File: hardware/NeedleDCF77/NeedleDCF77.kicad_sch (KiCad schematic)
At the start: 42 parts, among them J1 USB_C_Receptacle_USB2.0, U2 STM32L051C8Tx

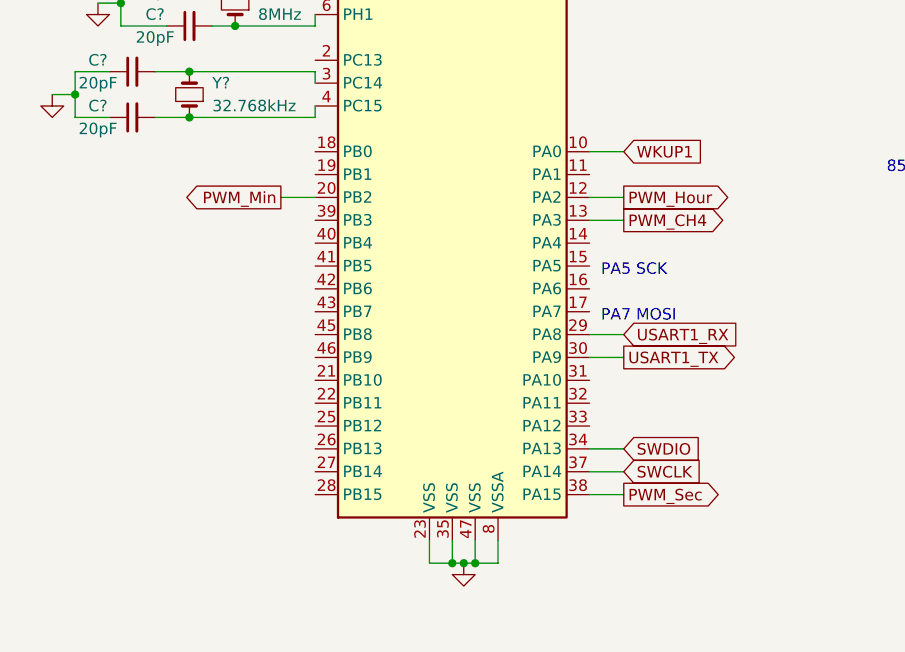
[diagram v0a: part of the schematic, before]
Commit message: Chose correct pins for PWM
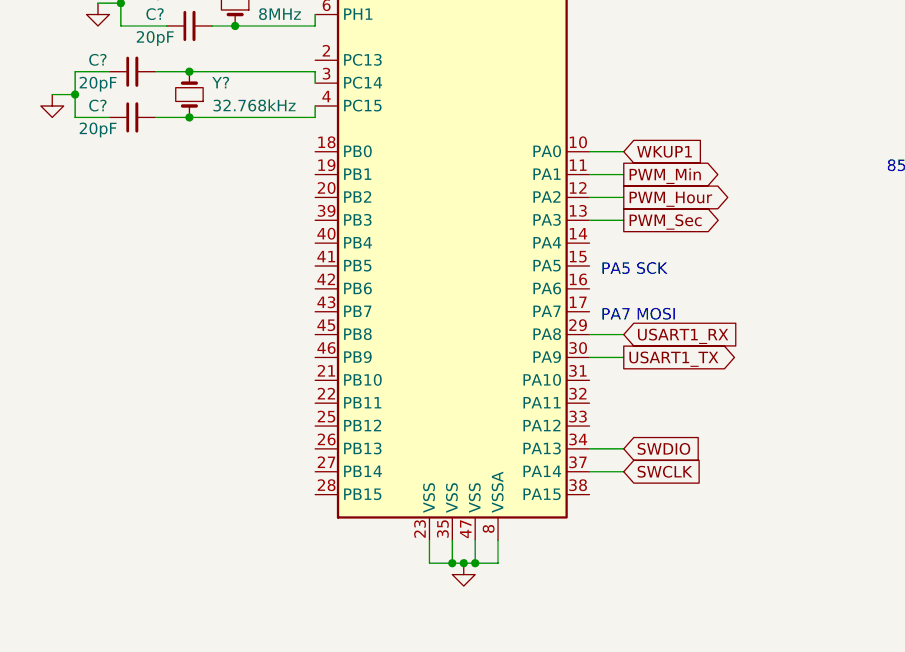
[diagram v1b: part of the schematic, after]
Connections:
- net PWM_CH4 is gone; now on net PWM_Sec: U2.13 (PA3)
- net PWM_Min: now also U2.11 (PA1); no longer U2.20 (PB2)
- net PWM_Sec: no longer U2.38 (PA15)

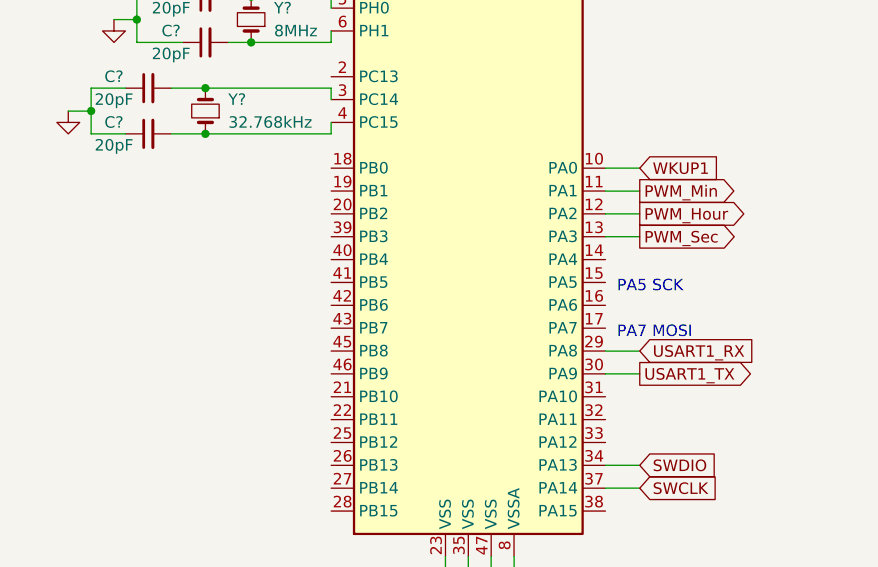
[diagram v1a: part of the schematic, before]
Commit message: Chose correct pins for SPI1
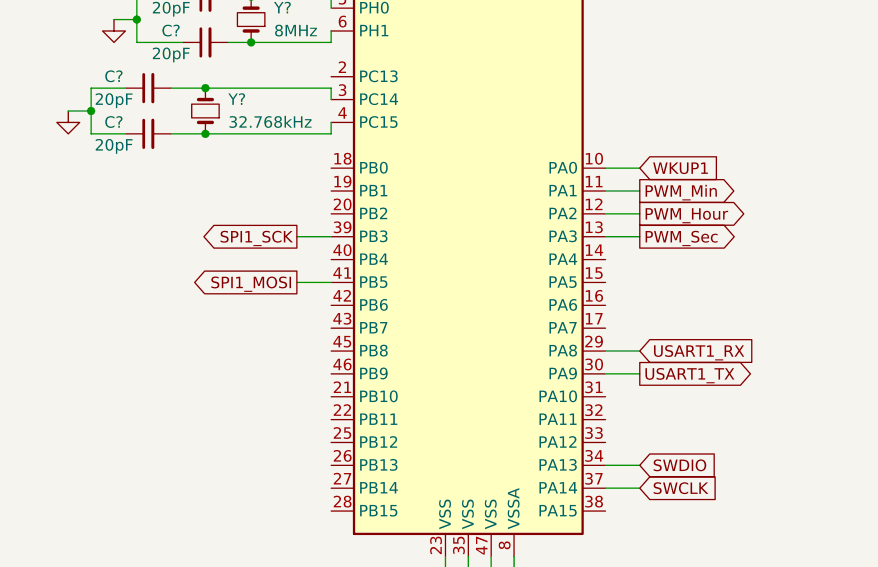
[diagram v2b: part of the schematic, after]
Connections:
- net SPI1_SCK: now reaches U2.39 (PB3)
- net SPI1_MOSI: now reaches U2.41 (PB5)
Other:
- note removed: "PA5 SCK"
- note removed: "PA7 MOSI"
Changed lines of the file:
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@@
+    (stroke (width 0) (type default))
+  )
+  (wire (pts (xy 157.48 147.32) (xy 161.29 147.32))
     (stroke (width 0) (type default))
   )
@@
   )
   (wire (pts (xy 254 152.4) (xy 254 154.94))
+    (stroke (width 0) (type default))
+  )
+  (wire (pts (xy 157.48 142.24) (xy 161.29 142.24))
     (stroke (width 0) (type default))
   )
@@
     (effects (font (size 1.27 1.27)) (justify left bottom))
   )
-  (text "PA5 SCK" (at 193.04 148.59 0)
-    (effects (font (size 1.27 1.27)) (justify left bottom))
-  )
   (text "On second PS create 5V to power VFD filament driver,\n and use linear regulator to 3v3 for ex on DCF77, or pending\n"
     (at 189.23 62.23 0)
     (effects (font (size 1.27 1.27)) (justify left bottom))
   )
-  (text "PA7 MOSI" (at 193.04 153.67 0)
-    (effects (font (size 1.27 1.27)) (justify left bottom))
-  )
   (text "85C1 50uA Resistance ~ 3.33kOma" (at 224.79 137.16 0)
     (effects (font (size 1.27 1.27)) (justify left bottom))
@@
     )
   )
+  (global_label "SPI1_SCK" (shape output) (at 157.48 142.24 180) (fields_autoplaced)
+    (effects (font (size 1.27 1.27)) (justify right))
+    (property "Intersheetrefs" "${INTERSHEET_REFS}" (at 145.5633 142.24 0)
+      (effects (font (size 1.27 1.27)) (justify right) hide)
+    )
+  )
   (global_label "PWM_Hour" (shape input) (at 250.19 139.7 180) (fields_autoplaced)
     (effects (font (size 1.27 1.27)) (justify right))
@@
     )
   )
+  (global_label "SPI1_MOSI" (shape output) (at 157.48 147.32 180) (fields_autoplaced)
+    (effects (font (size 1.27 1.27)) (justify right))
+    (property "Intersheetrefs" "${INTERSHEET_REFS}" (at 144.7166 147.32 0)
+      (effects (font (size 1.27 1.27)) (justify right) hide)
+    )
+  )

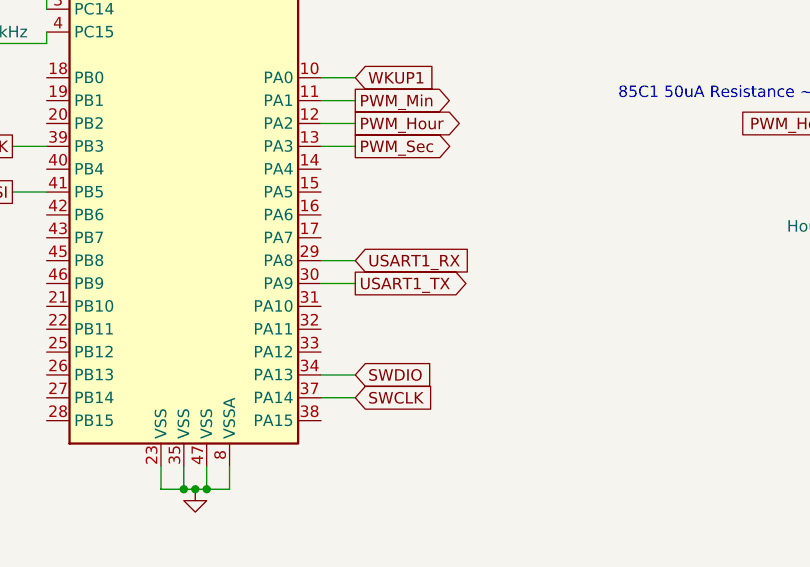
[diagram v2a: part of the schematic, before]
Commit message: Chose correct pins for UART1
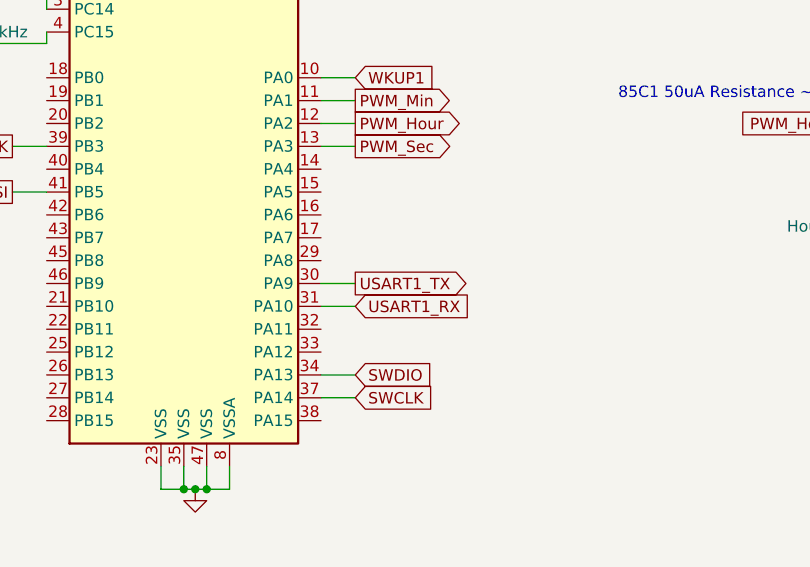
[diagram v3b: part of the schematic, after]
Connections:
- net USART1_RX: now also U2.31 (PA10); no longer U2.29 (PA8)
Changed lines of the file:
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@@
+    (stroke (width 0) (type default))
+  )
+  (wire (pts (xy 191.77 160.02) (xy 195.58 160.02))
     (stroke (width 0) (type default))
   )
@@
   )
   (wire (pts (xy 189.23 36.83) (xy 191.77 36.83))
-    (stroke (width 0) (type default))
-  )
-  (wire (pts (xy 191.77 154.94) (xy 195.58 154.94))
     (stroke (width 0) (type default))
   )
@@
     )
   )
-  (global_label "USART1_RX" (shape input) (at 195.58 154.94 0) (fields_autoplaced)
-    (effects (font (size 1.27 1.27)) (justify left))
-    (property "Intersheetrefs" "${INTERSHEET_REFS}" (at 208.516 154.8606 0)
-      (effects (font (size 1.27 1.27)) (justify left) hide)
-    )
+  (global_label "USART1_RX" (shape input) (at 195.58 160.02 0) (fields_autoplaced)
+    (effects (font (size 1.27 1.27)) (justify left))
+    (property "Intersheetrefs" "${INTERSHEET_REFS}" (at 208.516 159.9406 0)
+      (effects (font (size 1.27 1.27)) (justify left) hide)
+    )

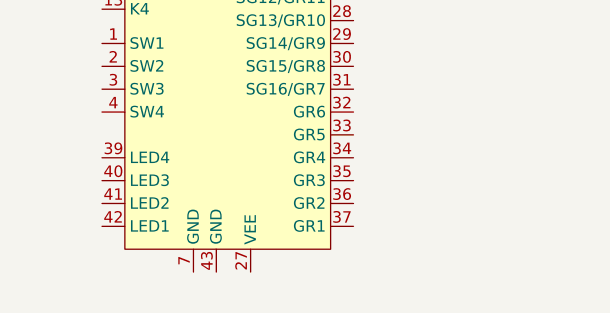
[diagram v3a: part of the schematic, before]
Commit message: Add ground to PT6312
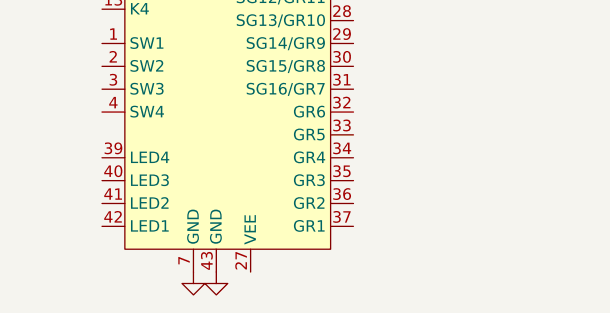
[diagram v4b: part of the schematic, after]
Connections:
- net GND: now also U?.43 (GND), U?.7 (GND)
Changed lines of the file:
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@@
+    )
+  )
+  (symbol (lib_id "power:GND") (at 48.26 187.96 0) (unit 1)
+    (in_bom yes) (on_board yes) (dnp no) (fields_autoplaced)
+    (property "Reference" "#PWR02" (at 48.26 194.31 0)
+      (effects (font (size 1.27 1.27)) hide)
+    )
+    (property "Value" "GND" (at 48.26 193.04 0)
+      (effects (font (size 1.27 1.27)) hide)
+    )
+    (property "Footprint" "" (at 48.26 187.96 0)
+      (effects (font (size 1.27 1.27)) hide)
+    )
+    (property "Datasheet" "" (at 48.26 187.96 0)
+      (effects (font (size 1.27 1.27)) hide)
+    )
+    (pin "1")
+    (instances
+      (project "NeedleDCF77"
+        (path "/9538e4ed-27e6-4c37-b989-9859dc0d49e8"
+          (reference "#PWR02") (unit 1)
+        )
+      )
     )
   )
@@
         )
       )
+    )
+  )
+  (symbol (lib_id "power:GND") (at 45.72 187.96 0) (unit 1)
+    (in_bom yes) (on_board yes) (dnp no) (fields_autoplaced)
+    (property "Reference" "#PWR01" (at 45.72 194.31 0)
+      (effects (font (size 1.27 1.27)) hide)
+    )
+    (property "Value" "GND" (at 45.72 193.04 0)
+      (effects (font (size 1.27 1.27)) hide)
+    )
+    (property "Footprint" "" (at 45.72 187.96 0)
+      (effects (font (size 1.27 1.27)) hide)
+    )
+    (property "Datasheet" "" (at 45.72 187.96 0)
+      (effects (font (size 1.27 1.27)) hide)
+    )
+    (pin "1")
+    (instances
+      (project "NeedleDCF77"
+        (path "/9538e4ed-27e6-4c37-b989-9859dc0d49e8"
+          (reference "#PWR01") (unit 1)
+        )
+      )

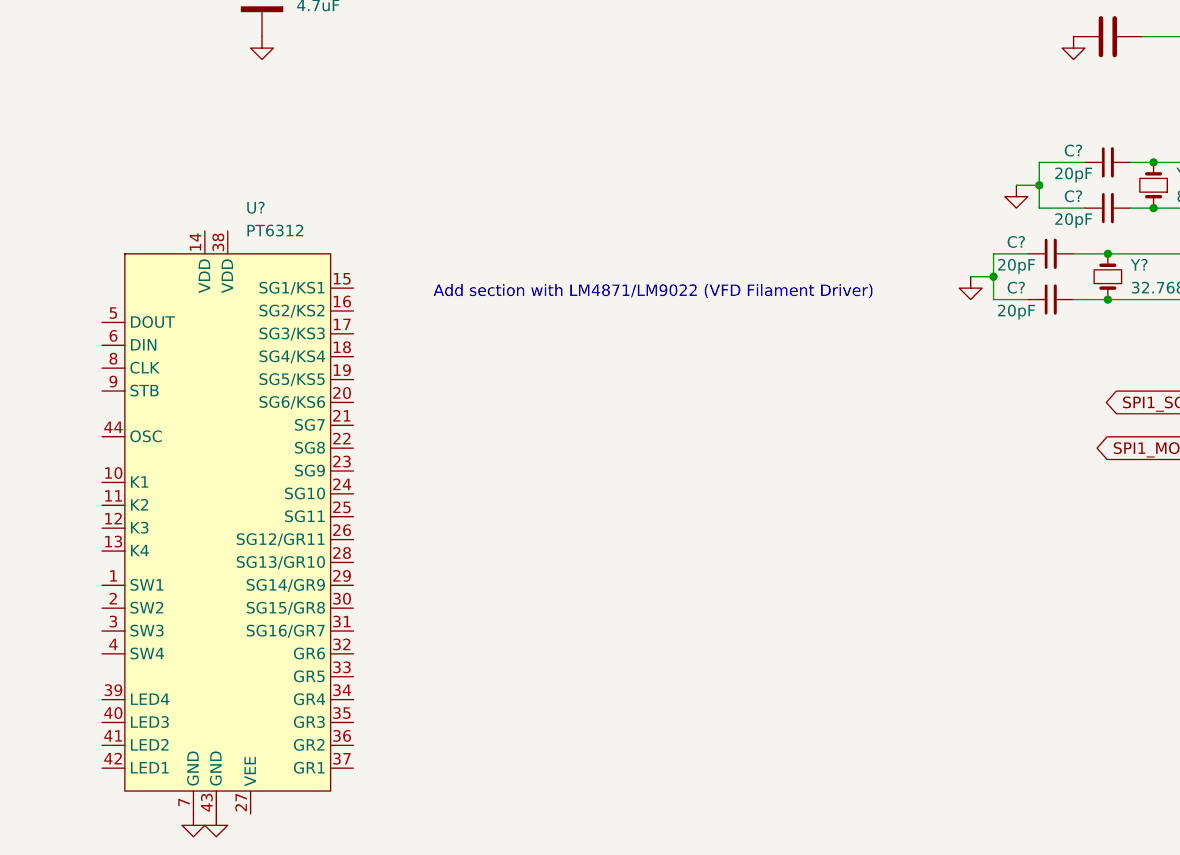
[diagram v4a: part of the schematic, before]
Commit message: Create Symbol for LM4871 and add it to schematic
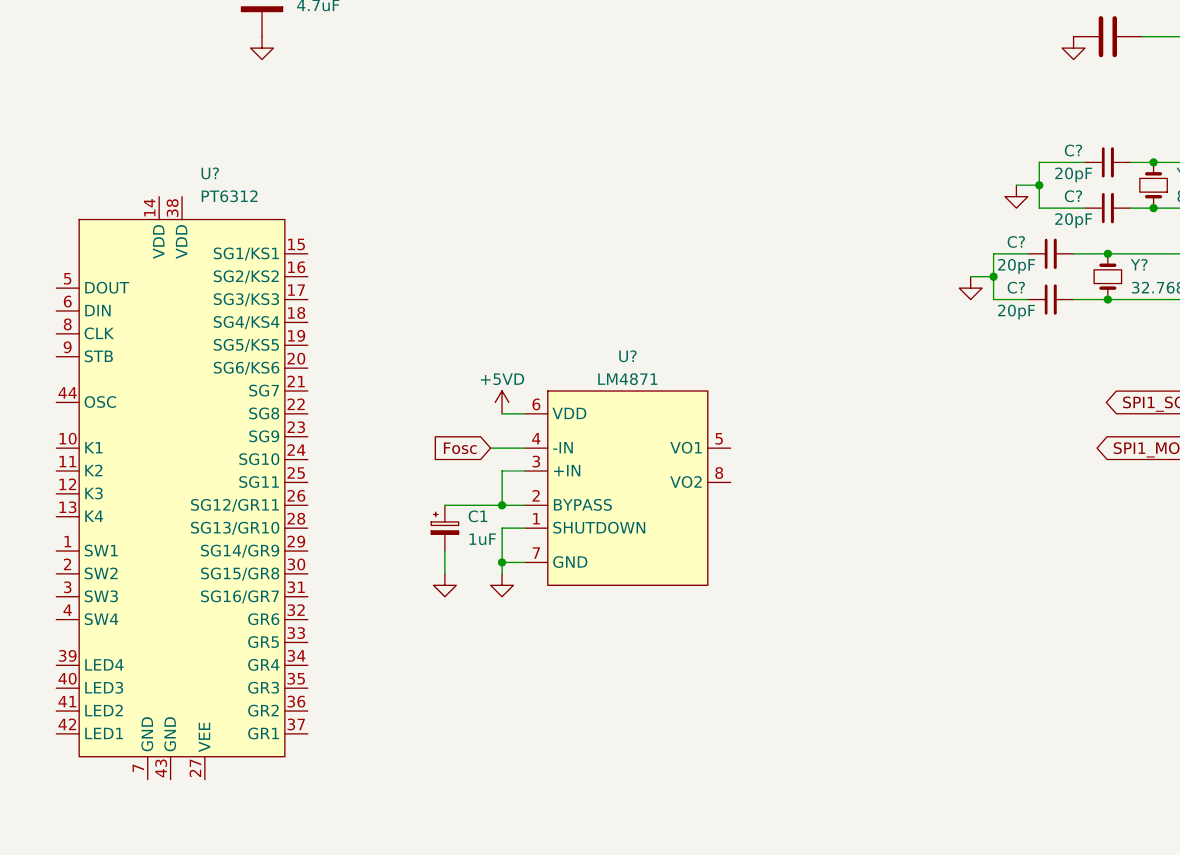
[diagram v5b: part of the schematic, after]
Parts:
- added C1: 1uF, symbol Device:C_Polarized_Small
- added U?: LM4871, Package_SO:SOIC-8_3.9x4.9mm_P1.27mm, symbol VFD_Driver:LM4871
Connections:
- net GND: now also C1.2, U?.1 (SHUTDOWN), U?.7 (GND); no longer U?.43 (GND), U?.7 (GND)
- new net: C1.1, U?.2 (BYPASS), U?.3 (+IN)
- new net +5VD: U?.6 (VDD)
- new net Fosc: U?.4 (-IN)
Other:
- note removed: "Add section with LM4871/LM9022 (VFD Filament Driver)"
- moved on the sheet: U?
